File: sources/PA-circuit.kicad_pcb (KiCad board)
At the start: 2 copper layers, 45.4 x 37.1 mm, 26 parts, among them J1 133-3701-311, J2 133-3701-311, J2 Conn_01x04_Female, J3 Conn_01x01_Female, U1 MMZ09332BT1

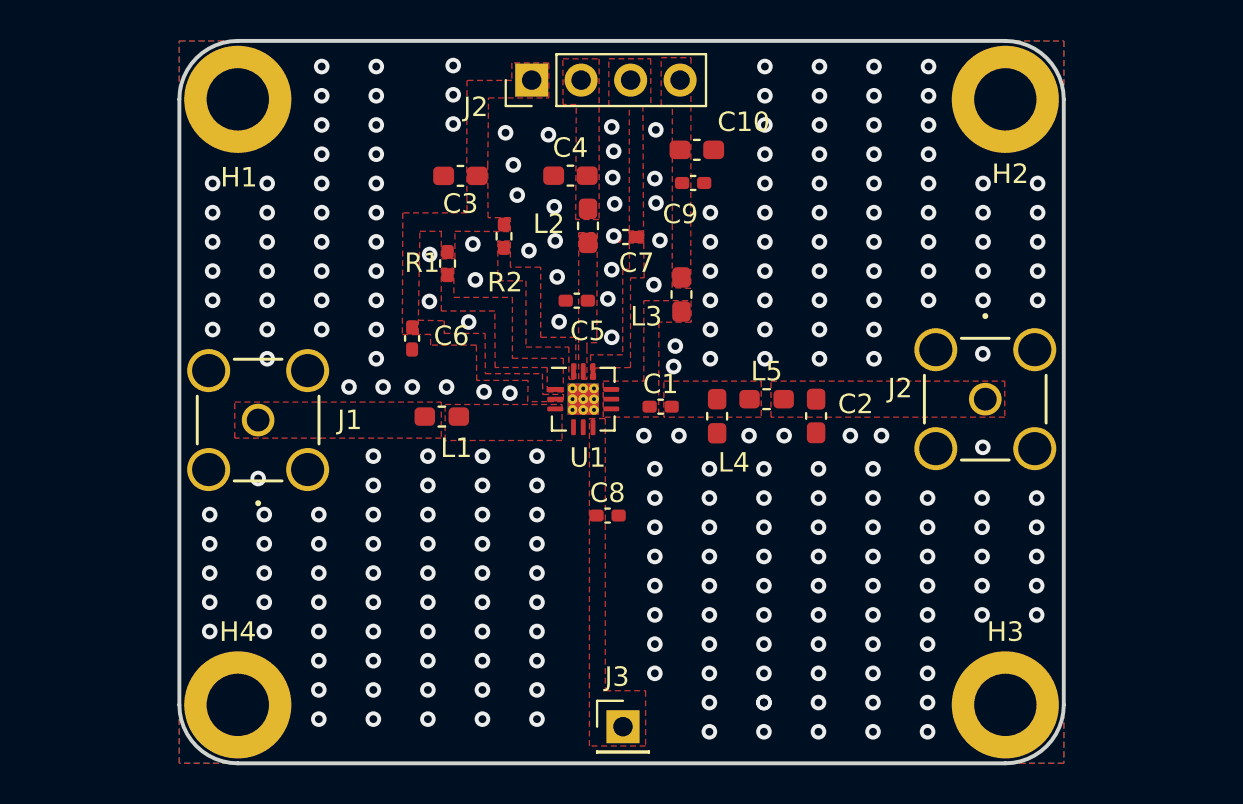
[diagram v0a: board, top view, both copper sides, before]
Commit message: updating rf connector and lib
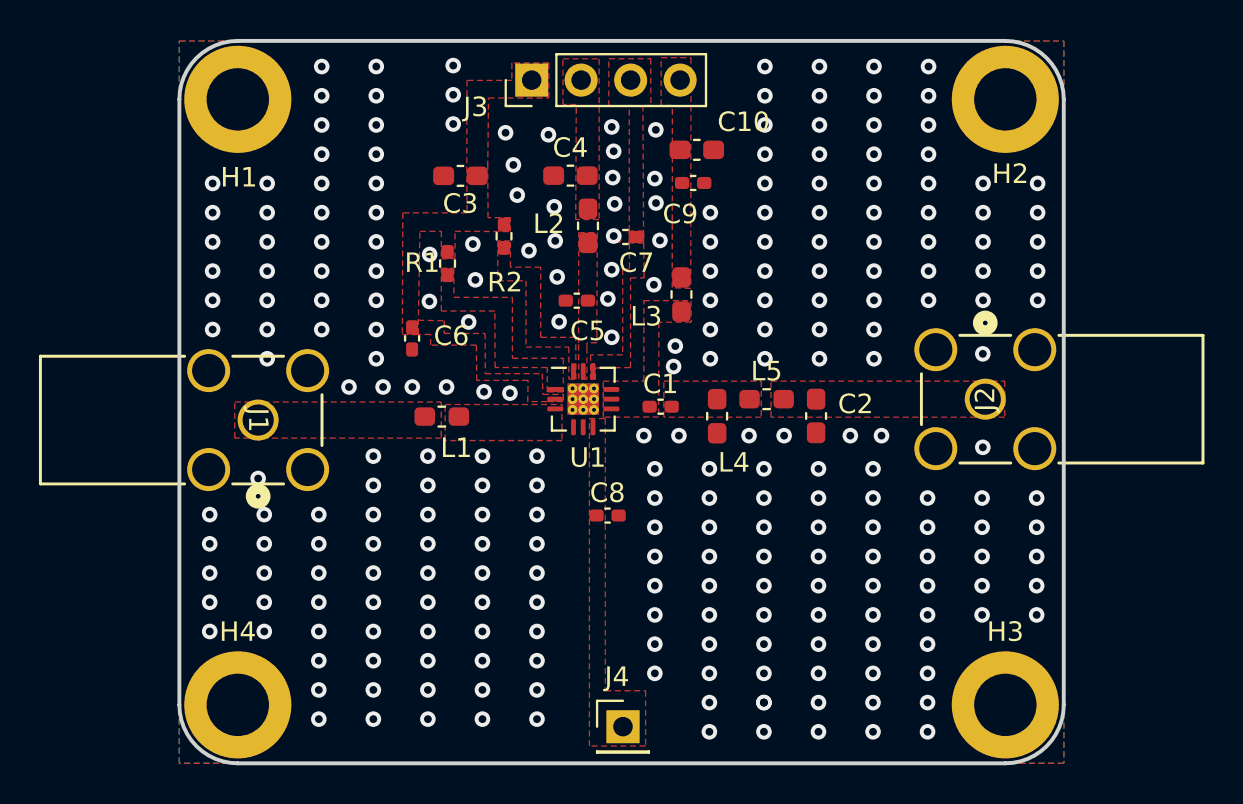
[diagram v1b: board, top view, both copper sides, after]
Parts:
- J1, J2: footprint 133-3701-311:133-3701-311 -> 2016504-1:2016504-1
- renumbered J2 to J3, J3 to J4

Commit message: finishing layout
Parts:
- added G***: LOGO, lib:spacelab-logo, F.Cu at (79.2, 67.3)
- added G***: LOGO, lib:scorp, F.Cu at (102.0, 72.5)
- J1: value 133-3701-311 -> 2484782-1
- J3: value Conn_01x04_Female -> Conn_01x05; footprint Connector_PinHeader_2.54mm:PinHeader_1x04_P2.54mm_Vertical -> Connector_PinHeader_2.54mm:PinHeader_1x05_P2.54mm_Vertical
- J4: renamed from J2; value 133-3701-311 -> 2484782-1
- moved J3 0.08 mm to (84.4, 42.1)
- renumbered C3 to C1, C2 to C10, C6 to C2, C7 to C3, C5 to C4, C8 to C5, C4 to C6, C1 to C7, C9 to C8, C10 to C9, H4 to H1, H1 to H3, H3 to H4, J4 to J2
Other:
- board text added: "TMTC PA Test Board v1.0"
